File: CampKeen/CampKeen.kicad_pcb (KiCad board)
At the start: 4 copper layers, 177.8 x 142.2 mm, 194 parts, among them IC1 LM2597MX-ADJ_NOPB, IC2 LM2670SX-5.0_NOPB, IC3 DS3231SN#, IC4 INA849DR, IC5 LM2904N_NOPB, J1 Vin, J2 CAC, J3 VAC, J4 Screw_Terminal_01x04, J5 GenEnclosure, J6 GenHeadL, J7 GenHeadR, K1 DIP05-1A72-12L, K2 DIP05-1A72-12L, K3 DIP05-1A72-12L, K4 DIP05-1A72-12L, P1 Power, P10 CONN_01X01, P11 CONN_01X01, P12 CONN_01X01, P13 CONN_01X01, P2 Analog, P3 Analog, P4 Digital, P5 PWM, P6 PWM, P7 Communication, P8 CONN_01X01, P9 CONN_01X01, Q1 BC547, Q10 2N7000, Q11 2N7000, Q12 2N7000, Q13 2N7000, Q14 2N7000, Q15 IRF510, Q16 2N7000, Q17 IRF510, Q18 2N7000, Q19 IRF510, Q2 2N7000, Q20 2N7000, Q21 IRF510, Q22 BC547, Q23 2N7000, Q24 IRF510, Q25 2N7000, Q26 2N7000, Q27 IRF510, Q28 2N7000, Q29 IRF510, Q3 2N7000, Q30 2N7000, Q31 IRF510, Q32 BC547, Q33 2N7000, Q35 2N7000, Q36 IRF510, Q37 2N7000, Q38 IRF510, Q39 IRF510, Q4 2N7000, Q40 IRF9Z34NPBF, Q5 2N7000, Q6 BC547, Q7 2N7000, Q8 2N7000, Q9 2N7000, T1 F24-045-C2, U1 TL431LP, U2 MAX232

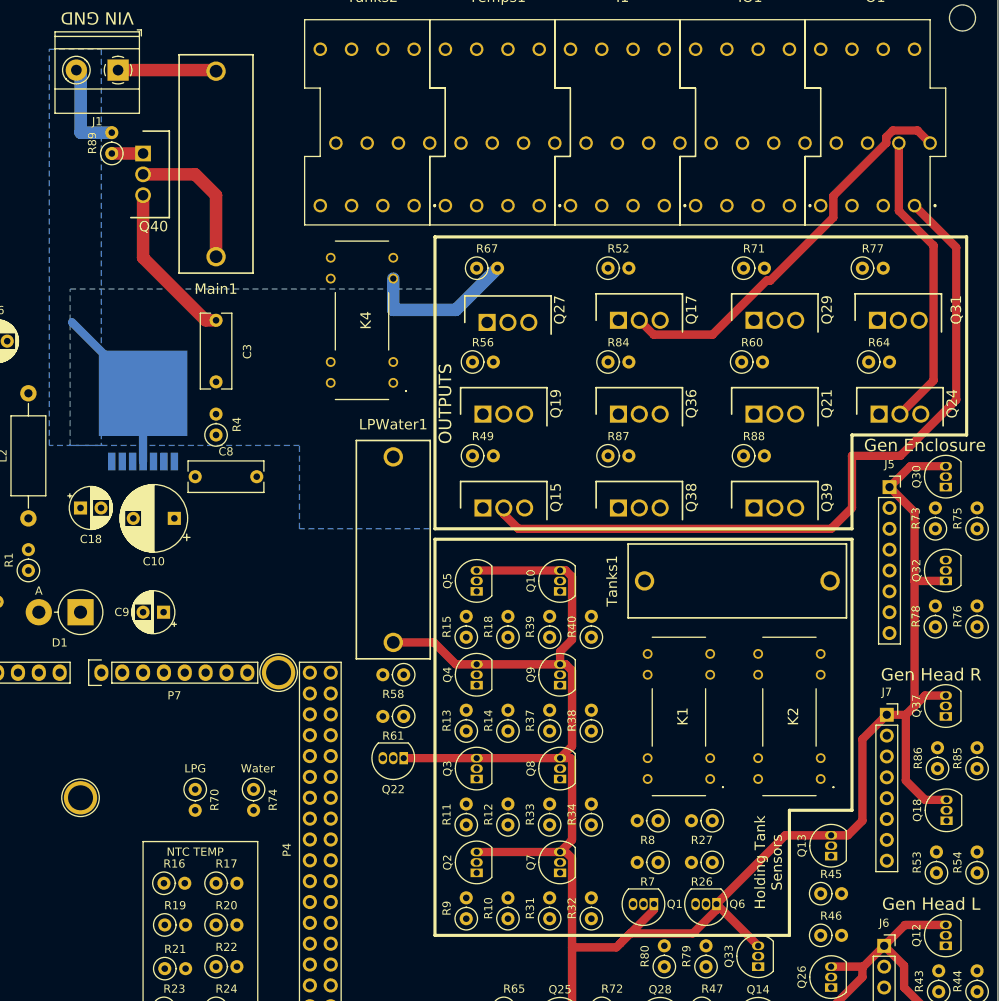
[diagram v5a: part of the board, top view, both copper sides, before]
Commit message: before removing my homegrown AC monitoring stuff.
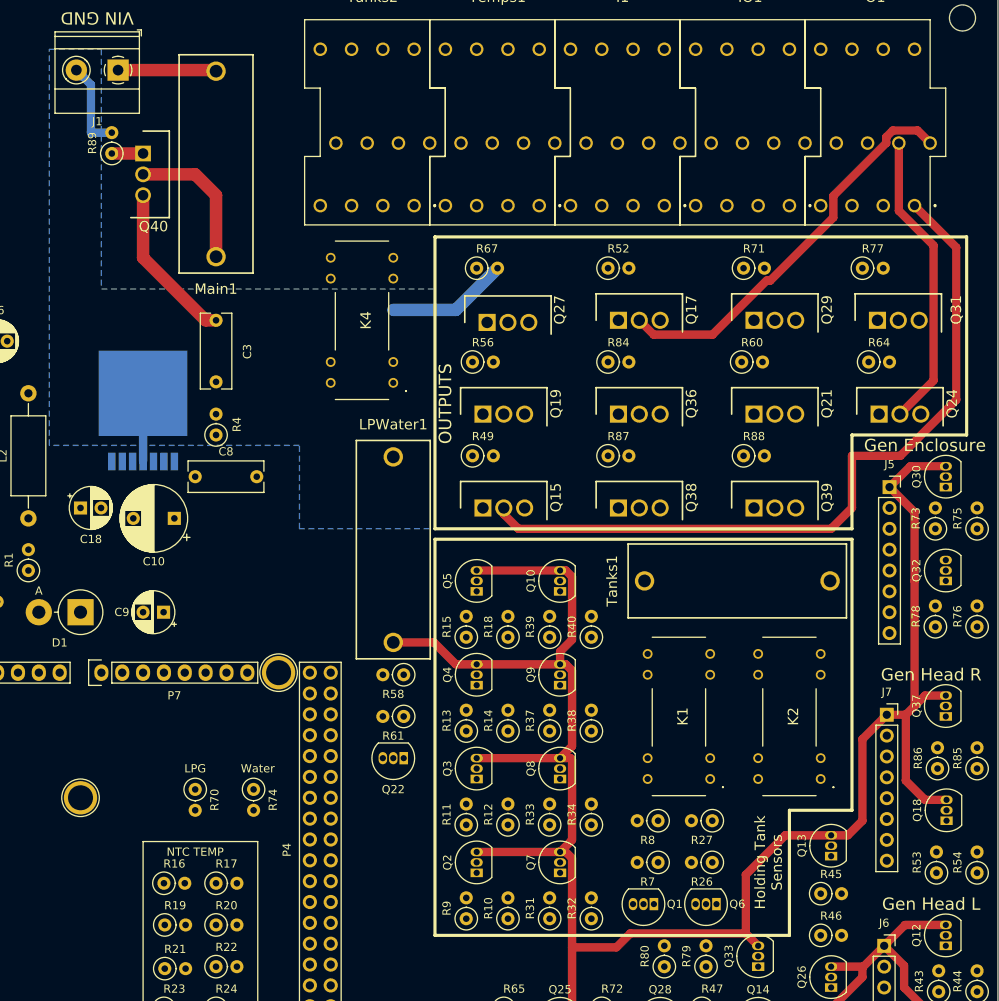
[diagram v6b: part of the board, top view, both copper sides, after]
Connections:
- K4 pad 2: Net-(K4-Pad2) -> +5V
- K4 pad 6: GND -> Net-(K4-Pad6)
- Q22 pad 1: +5V -> Net-(K4-Pad6)
- Q22 pad 3: Net-(K4-Pad2) -> GND
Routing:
- net +5V: track 358.8 -> 338.3 mm
- net GND: track 52.9 -> 36.8 mm
- removed copper zone on B.Cu, net (none)

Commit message: files submitted for Fab Verions 0.5
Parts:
- removed BR1: DF04M, SamacSys_Parts:DIP825W58P510L828H330Q4N
- removed C11: 10uF, Capacitor_THT:C_Rect_L9.0mm_W3.6mm_P7.50mm_MKT
- removed C12: 2.2uF, Capacitor_THT:CP_Radial_D4.0mm_P2.00mm
- removed C13: 10nF, Capacitor_THT:C_Disc_D7.5mm_W5.0mm_P5.00mm
- removed K3: DIP05-1A72-12L, SamacSys_Parts:DIP051A7212L
- removed R25: 33, Resistor_THT:R_Axial_DIN0207_L6.3mm_D2.5mm_P10.16mm_Horizontal
- removed R29: 1K, Resistor_THT:R_Axial_DIN0207_L6.3mm_D2.5mm_P2.54mm_Vertical
- removed R30: 1M, Resistor_THT:R_Axial_DIN0207_L6.3mm_D2.5mm_P2.54mm_Vertical
- removed R36: 180k, Resistor_THT:R_Axial_DIN0207_L6.3mm_D2.5mm_P2.54mm_Vertical
- removed R90: 100k, Resistor_THT:R_Axial_DIN0207_L6.3mm_D2.5mm_P2.54mm_Vertical
- removed T1: F24-045-C2, SamacSys_Parts:F24045C2
- removed U1: TL431LP, Package_TO_SOT_THT:TO-92_Inline
- removed VACFuse1: VAC, SamacSys_Parts:BK_HTC-15M
- IC2, R35: moved to F.Cu
- IC4: value INA849DR -> CD74HC4050ME4; footprint SamacSys_Parts:SOIC127P600X175-8N -> SamacSys_Parts:SOIC127P600X175-16N
- IC5: value LM2904N_NOPB -> TL071CP; moved to F.Cu
- J2: value CAC -> CircuitSetupsSplitPhase; footprint TerminalBlock_Phoenix:TerminalBlock_Phoenix_MKDS-1,5-2-5.08_1x02_P5.08mm_Horizontal -> Connector_PinSocket_2.54mm:PinSocket_1x09_P2.54mm_Vertical
- J3: value VAC -> Vin
- R2, R3: footprint Resistor_THT:R_Axial_DIN0207_L6.3mm_D2.5mm_P2.54mm_Vertical -> Resistor_THT:R_Axial_DIN0204_L3.6mm_D1.6mm_P7.62mm_Horizontal
- R82: value 20K -> 19.2K; moved to F.Cu
- moved J4 109.7 mm to (52.6, 95.2), turned to 270 degrees
- moved J2 64.5 mm to (87.5, 89.5), turned to 270 degrees
- moved C7 49.5 mm to (104.6, 64.8)
- moved J3 44.5 mm to (108.5, 24.1)
- moved IC4 42.2 mm to (65.3, 78.7), turned to 90 degrees
- moved R28 41.6 mm to (97.0, 19.1), turned to 180 degrees
- moved C4 37.5 mm to (103.4, 73.7)
- moved IC5 36.3 mm to (86.9, 25.4), turned to 0 degrees
- moved R1 35.8 mm to (89.4, 54.6), turned to 270 degrees
- moved R82 35.3 mm to (97.0, 24.1)
- moved R35 35.3 mm to (97.0, 29.2)
- moved C1 33.2 mm to (103.4, 80.0)
- moved IC1 31.4 mm to (97.0, 57.1), turned to 0 degrees
- moved R3 29.5 mm to (80.5, 63.5), turned to 270 degrees
- moved C9 25.7 mm to (118.6, 66.0), turned to 0 degrees
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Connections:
- IC4 pad 1: Net-(C11-Pad1) -> +3V3
- IC4 pad 2: (no net) -> /SCLK
- IC4 pad 3: (no net) -> /52(SCK)
- IC4 pad 4: Net-(C11-Pad2) -> /50(MISO)
- IC4 pad 5: GND -> /50(MISO)
- IC4 pad 6: Net-(IC4-Pad6) -> /51(MOSI)
- IC4 pad 7: /A12 -> /51(MOSI)
- IC4 pad 8: +5V -> GND
- IC5 pad 1: Net-(IC4-Pad6) -> (no net)
- IC5 pad 2: Net-(IC4-Pad6) -> /A0
- IC5 pad 5: Net-(IC5-Pad5) -> (no net)
- IC5 pad 7: /A0 -> +5V
- IC5 pad 8: +5V -> (no net)
- J2 pad 1: Net-(C11-Pad1) -> GND
- J2 pad 2: Net-(C11-Pad2) -> (no net)
- J3 pad 1: Net-(J3-Pad1) -> +12V
- J3 pad 2: Net-(J3-Pad2) -> GND
- P1 pad 4: (no net) -> +3V3
- P3 pad 4: /A11 -> (no net)
- P3 pad 5: /A12 -> (no net)
- Q35 pad 1: /41 -> Net-(Q35-Pad1)
- R28 pad 1: Net-(IC5-Pad5) -> Net-(IC5-Pad3)
- R82 pad 2: Net-(IC5-Pad5) -> Net-(IC5-Pad3)
- R83 pad 1: /41 -> Net-(Q35-Pad1)
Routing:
- net GND: track 36.8 -> 875.5 mm, vias 0 -> 3
- net +5V: track 338.3 -> 693.9 mm
- net /52(SCK): track 0.00 -> 262.3 mm, vias 0 -> 3
- net /50(MISO): track 0.00 -> 251.5 mm, vias 0 -> 1
- net /51(MOSI): track 0.00 -> 251.4 mm, vias 0 -> 1
- net +9V: track 0.00 -> 245.4 mm, vias 0 -> 2
- net Net-(IO1-Pad3): track 0.00 -> 211.9 mm, vias 0 -> 2
- net /A1: track 0.00 -> 207.6 mm, vias 0 -> 3
- net Net-(IO1-Pad2): track 0.00 -> 204.5 mm, vias 0 -> 2
- net Net-(IO1-Pad4): track 0.00 -> 201.2 mm, vias 0 -> 2
- net /A2: track 0.00 -> 198.7 mm, vias 0 -> 2
- net /2(**): track 0.00 -> 190.5 mm, vias 0 -> 2
- net /A4: track 0.00 -> 172.0 mm
- net Net-(I1-Pad12): track 0.00 -> 170.8 mm
- net /A13: track 0.00 -> 169.3 mm, vias 0 -> 3
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- added copper zone on F.Cu, net GND
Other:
- outline, holes or cut-outs redrawn
- board text added: "12V GND"
- board text added: "5V Power"
- board text added: "9V Power"
- board text added: "CircuitSetup.us Split Single Phase Energy Meter"
- board text added: "RS232"
- board text added: "Resistive Tank"
- board text added: "SDA SCL GND 5V"
- board text added: "Version: 0.5"
- board text added: "Voltage Sensor"
- board text added: "Vorticons are INVADING! RUN GET BILLY BLAZE! POGO AND RAY GUNS and don't foget your HELMET"
- board text removed: "AC Current"
- board text removed: "VAC Line Neut"
- board text removed: "Version: 0.3"

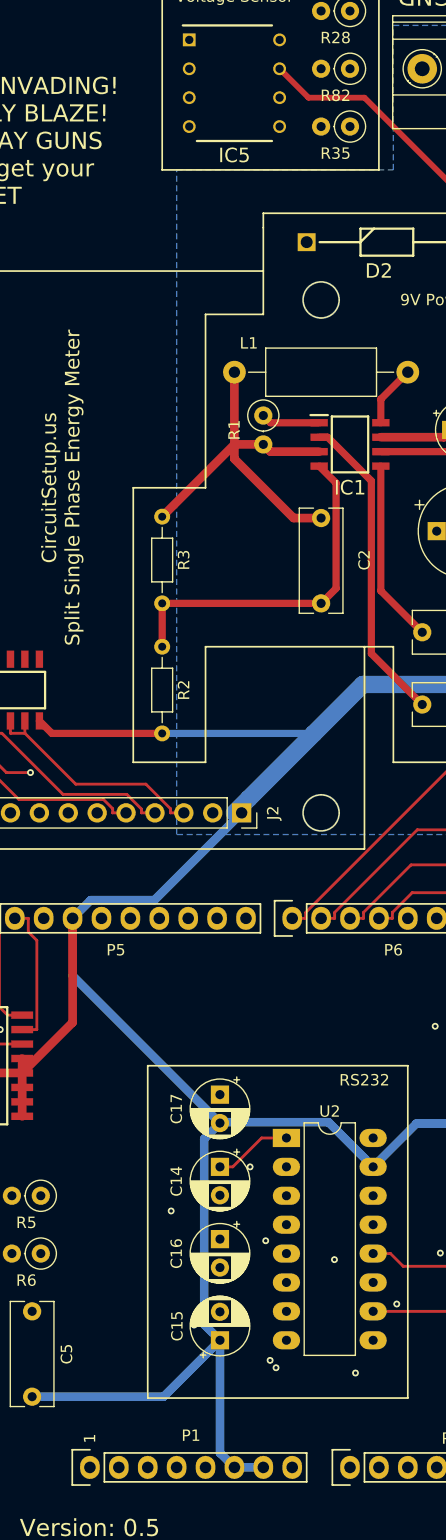
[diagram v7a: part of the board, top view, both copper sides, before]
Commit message: fixed the mistake on the RS232 driver.
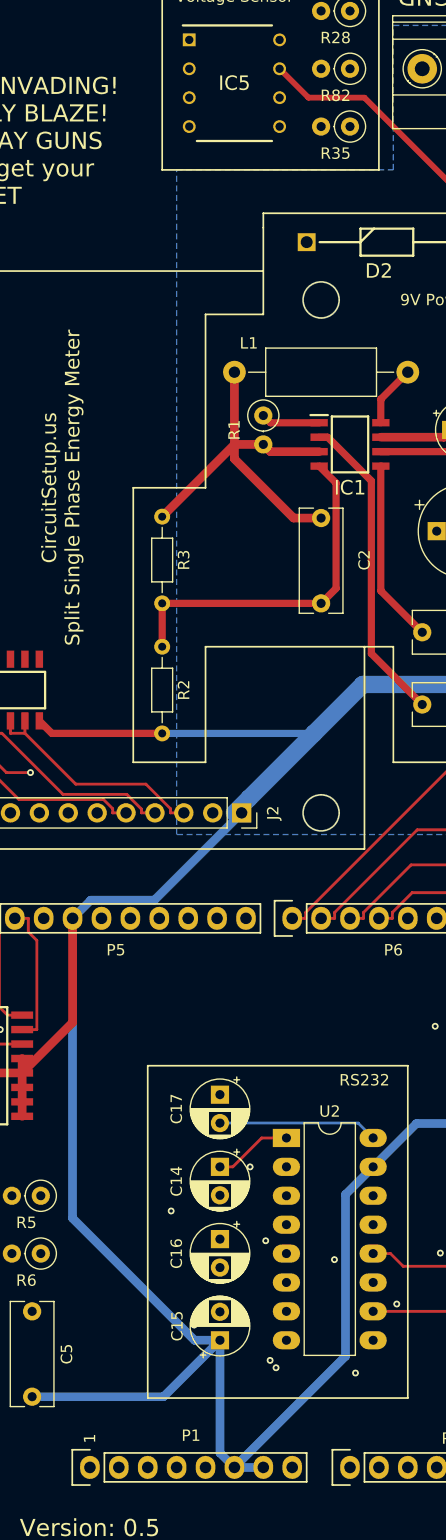
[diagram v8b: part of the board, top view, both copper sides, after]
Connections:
- C17 pad 2: GND -> +5V
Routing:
- net GND: track 875.5 -> 892.0 mm
- net +5V: track 693.9 -> 708.0 mm
